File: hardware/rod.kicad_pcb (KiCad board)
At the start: 2 copper layers, 11 parts, among them P1 CONN_01X12, P2 CONN_01X12, P3 GYRO, P4 DOTSTAR, SW1 SW_PUSH_R, SW2 SW_PUSH_G, SW3 SW_PUSH_B

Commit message: Updated PCB
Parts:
- removed BZ1: buzzer, Buzzers_Beepers:MagneticBuzzer_Kingstate_KCG0601
- removed P3: GYRO, Pin_Headers:Pin_Header_Straight_1x05
- added P5: USB_B, Connect:USB_B, F.Cu at (104.1, 170.2)
- P1, P2: value CONN_01X12 -> arduino_mini
- SW1: moved to B.Cu
- SW2: value SW_PUSH_G -> SW_PUSH_B; moved to B.Cu
- SW3: value SW_PUSH_B -> SW_PUSH_G; moved to B.Cu
- moved SW2 34.4 mm to (104.1, 130.8), turned to 90 degrees
- moved SW1 31.9 mm to (104.1, 113.0), turned to 90 degrees
- moved P1 29.6 mm to (119.4, 59.7)
- moved SW3 28.1 mm to (104.1, 148.6), turned to 90 degrees
- moved R1 24.0 mm to (119.4, 106.7), turned to 270 degrees
- moved P2 18.3 mm to (101.6, 59.7)
- moved R2 17.3 mm to (116.8, 123.2), turned to 270 degrees
- moved R3 14.5 mm to (119.4, 143.5), turned to 270 degrees
- moved P4 12.0 mm to (114.3, 49.5), turned to 270 degrees
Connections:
- P1 pad 5: Net-(P1-Pad5) -> A3
- P2 pad 4: GND -> Net-(P2-Pad4)
- P2 pad 6: e -> 3
- P4 pad 2: 6 -> 3
- P4 pad 3: 7 -> 2
- R1 pad 2: 4 -> 6
- R2 pad 2: 3 -> 5
- R3 pad 2: 2 -> 4
- SW1 pad 2: 4 -> 6
- SW2 pad 2: 3 -> 5
- SW3 pad 2: 2 -> 4
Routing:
- net PWR: track 0.00 -> 174.4 mm
- net GND: track 0.00 -> 170.9 mm
- net TX: track 0.00 -> 136.8 mm
- net RX: track 0.00 -> 129.0 mm
- net 4: track 0.00 -> 98.5 mm
- net 5: track 0.00 -> 72.8 mm
- net 6: track 0.00 -> 52.3 mm
- net 3: track 0.00 -> 30.0 mm
- net 2: track 0.00 -> 25.7 mm

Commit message: Updated PCB
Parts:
- moved P5 7.18 mm to (109.2, 175.3), turned to 270 degrees
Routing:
- net PWR: track 174.4 -> 211.3 mm
- net RX: track 129.0 -> 135.1 mm
- net TX: track 136.8 -> 140.4 mm
- net 6: track 52.3 -> 51.2 mm

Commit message: "Updated PCB"
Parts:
- moved R1 4.02 mm to (115.6, 108.0)
- moved R3 3.81 mm to (115.6, 143.5)
- moved R2 2.84 mm to (115.6, 125.7)
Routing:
- net GND: track 170.7 -> 162.9 mm
- net 6: track 51.2 -> 46.1 mm
- net 4: track 98.5 -> 94.7 mm
- net 5: track 72.8 -> 72.0 mm
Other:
- board outline added: 61 x 154.9 mm

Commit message: bak file created
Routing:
- net PWR: track 211.3 -> 176.5 mm
- net TX: track 140.4 -> 136.1 mm
- net GND: track 162.9 -> 159.3 mm
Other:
- board size 61 x 154.9 mm -> 40.6 x 149.9 mm
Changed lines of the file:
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@@
     (links 27)
     (no_connects 7)
-    (area 87.304999 41.584999 133.675002 190.735001)
+    (area 78.664999 35.484999 139.775001 190.575001)
     (thickness 1.6)
-    (drawings 4)
-    (tracks 93)
+    (drawings 6)
+    (tracks 94)
     (zones 0)
     (modules 10)
@@
       (outputformat 1)
       (mirror false)
-      (drillshape 1)
+      (drillshape 0)
       (scaleselection 1)
       (outputdirectory ""))
@@
     )
   )
-  (gr_line (start 78.74 190.5) (end 78.74 35.56) (angle 90) (layer Edge.Cuts) (width 0.15))
-  (gr_line (start 139.7 190.5) (end 78.74 190.5) (angle 90) (layer Edge.Cuts) (width 0.15))
-  (gr_line (start 139.7 35.56) (end 139.7 190.5) (angle 90) (layer Edge.Cuts) (width 0.15))
-  (gr_line (start 78.74 35.56) (end 139.7 35.56) (angle 90) (layer Edge.Cuts) (width 0.15))
-  (segment (start 115.57 125.73) (end 119.38 121.92) (width 0.25) (layer F.Cu) (net 2) (status 400000))
-  (segment (start 118.11 107.95) (end 115.57 107.95) (width 0.25) (layer F.Cu) (net 2) (status 800000))
+  (gr_line (start 91.44 190.5) (end 128.27 190.5) (angle 90) (layer Edge.Cuts) (width 0.15))
+  (gr_line (start 87.63 40.64) (end 128.27 40.64) (angle 90) (layer Edge.Cuts) (width 0.15))
+  (gr_line (start 87.63 190.5) (end 91.44 190.5) (angle 90) (layer Edge.Cuts) (width 0.15))
+  (gr_line (start 87.63 40.64) (end 87.63 190.5) (angle 90) (layer Edge.Cuts) (width 0.15))
+  (gr_line (start 128.27 187.96) (end 128.27 190.5) (angle 90) (layer Edge.Cuts) (width 0.15))
+  (gr_line (start 128.27 40.64) (end 128.27 187.96) (angle 90) (layer Edge.Cuts) (width 0.15))
+  (segment (start 114.3 49.53) (end 120.65 49.53) (width 0.25) (layer F.Cu) (net 2) (status 400000))
+  (segment (start 120.65 62.23) (end 119.38 62.23) (width 0.25) (layer F.Cu) (net 2) (status 800000))
+  (segment (start 121.92 60.96) (end 120.65 62.23) (width 0.25) (layer F.Cu) (net 2))
+  (segment (start 121.92 50.8) (end 121.92 60.96) (width 0.25) (layer F.Cu) (net 2))
+  (segment (start 120.65 49.53) (end 121.92 50.8) (width 0.25) (layer F.Cu) (net 2))
+  (segment (start 115.57 125.73) (end 119.38 121.92) (width 0.25) (layer F.Cu) (net 2))
+  (segment (start 118.11 107.95) (end 115.57 107.95) (width 0.25) (layer F.Cu) (net 2))
   (segment (start 119.38 109.22) (end 118.11 107.95) (width 0.25) (layer F.Cu) (net 2))
   (segment (start 119.38 121.92) (end 119.38 109.22) (width 0.25) (layer F.Cu) (net 2))
@@
   (segment (start 116.84 62.23) (end 119.38 62.23) (width 0.25) (layer F.Cu) (net 2))
   (segment (start 115.57 63.5) (end 116.84 62.23) (width 0.25) (layer F.Cu) (net 2))
-  (segment (start 114.3 49.53) (end 121.92 49.53) (width 0.25) (layer F.Cu) (net 2))
-  (segment (start 121.92 62.23) (end 119.38 62.23) (width 0.25) (layer F.Cu) (net 2))
-  (segment (start 124.46 59.69) (end 121.92 62.23) (width 0.25) (layer F.Cu) (net 2))
-  (segment (start 124.46 52.07) (end 124.46 59.69) (width 0.25) (layer F.Cu) (net 2))
-  (segment (start 121.92 49.53) (end 124.46 52.07) (width 0.25) (layer F.Cu) (net 2))
-  (segment (start 113.03 46.99) (end 115.57 44.45) (width 0.25) (layer F.Cu) (net 5))
+  (segment (start 120.65 44.45) (end 125.73 49.53) (width 0.25) (layer F.Cu) (net 5))
+  (segment (start 125.73 64.77) (end 123.19 67.31) (width 0.25) (layer F.Cu) (net 5))
+  (segment (start 125.73 49.53) (end 125.73 64.77) (width 0.25) (layer F.Cu) (net 5))
+  (segment (start 119.38 45.72) (end 124.46 50.8) (width 0.25) (layer F.Cu) (net 5))
+  (segment (start 124.46 63.5) (end 121.92 66.04) (width 0.25) (layer F.Cu) (net 5))
+  (segment (start 124.46 50.8) (end 124.46 63.5) (width 0.25) (layer F.Cu) (net 5))
+  (segment (start 106.68 45.72) (end 107.95 44.45) (width 0.25) (layer F.Cu) (net 5))
+  (segment (start 107.95 44.45) (end 120.65 44.45) (width 0.25) (layer F.Cu) (net 5))
+  (segment (start 114.3 45.72) (end 119.38 45.72) (width 0.25) (layer F.Cu) (net 5))
+  (segment (start 113.03 46.99) (end 114.3 45.72) (width 0.25) (layer F.Cu) (net 5))
   (segment (start 120.65 66.04) (end 119.38 67.31) (width 0.25) (layer F.Cu) (net 5))
-  (segment (start 125.73 66.04) (end 120.65 66.04) (width 0.25) (layer F.Cu) (net 5))
-  (segment (start 130.81 60.96) (end 125.73 66.04) (width 0.25) (layer F.Cu) (net 5))
-  (segment (start 130.81 46.99) (end 130.81 60.96) (width 0.25) (layer F.Cu) (net 5))
-  (segment (start 128.27 44.45) (end 130.81 46.99) (width 0.25) (layer F.Cu) (net 5))
-  (segment (start 115.57 44.45) (end 128.27 44.45) (width 0.25) (layer F.Cu) (net 5))
-  (segment (start 106.68 46.99) (end 106.68 44.45) (width 0.25) (layer F.Cu) (net 5))
-  (segment (start 129.54 67.31) (end 119.38 67.31) (width 0.25) (layer F.Cu) (net 5))
-  (segment (start 133.35 63.5) (end 129.54 67.31) (width 0.25) (layer F.Cu) (net 5))
-  (segment (start 133.35 44.45) (end 133.35 63.5) (width 0.25) (layer F.Cu) (net 5))
-  (segment (start 130.81 41.91) (end 133.35 44.45) (width 0.25) (layer F.Cu) (net 5))
-  (segment (start 109.22 41.91) (end 130.81 41.91) (width 0.25) (layer F.Cu) (net 5))
-  (segment (start 106.68 44.45) (end 109.22 41.91) (width 0.25) (layer F.Cu) (net 5))
+  (segment (start 121.92 66.04) (end 120.65 66.04) (width 0.25) (layer F.Cu) (net 5))
+  (segment (start 106.68 46.99) (end 106.68 45.72) (width 0.25) (layer F.Cu) (net 5))
+  (segment (start 123.19 67.31) (end 119.38 67.31) (width 0.25) (layer F.Cu) (net 5))
   (segment (start 106.68 49.53) (end 106.68 46.99) (width 0.25) (layer F.Cu) (net 5))
   (segment (start 106.68 154.94) (end 110.49 158.75) (width 0.25) (layer F.Cu) (net 5))
@@
   (segment (start 106.68 72.39) (end 101.6 72.39) (width 0.25) (layer F.Cu) (net 21))
   (segment (start 111.76 67.31) (end 106.68 72.39) (width 0.25) (layer F.Cu) (net 21))
+  (segment (start 95.25 59.69) (end 90.17 64.77) (width 0.25) (layer F.Cu) (net 23))
+  (segment (start 90.17 167.64) (end 91.44 168.91) (width 0.25) (layer F.Cu) (net 23))
+  (segment (start 90.17 64.77) (end 90.17 167.64) (width 0.25) (layer F.Cu) (net 23))
   (segment (start 106.68 175.26) (end 104.14 172.72) (width 0.25) (layer F.Cu) (net 23))
-  (segment (start 95.25 172.72) (end 87.63 165.1) (width 0.25) (layer F.Cu) (net 23))
-  (segment (start 87.63 165.1) (end 87.63 63.5) (width 0.25) (layer F.Cu) (net 23))
-  (segment (start 87.63 63.5) (end 91.44 59.69) (width 0.25) (layer F.Cu) (net 23))
-  (segment (start 91.44 59.69) (end 101.6 59.69) (width 0.25) (layer F.Cu) (net 23))
+  (segment (start 95.25 172.72) (end 91.44 168.91) (width 0.25) (layer F.Cu) (net 23))
   (segment (start 104.14 172.72) (end 95.25 172.72) (width 0.25) (layer F.Cu) (net 23))
+  (segment (start 95.25 59.69) (end 101.6 59.69) (width 0.25) (layer F.Cu) (net 23))
   (segment (start 106.13898 172.17898) (end 107.95 173.99) (width 0.25) (layer F.Cu) (net 24))
   (segment (start 101.6 62.23) (end 95.25 62.23) (width 0.25) (layer F.Cu) (net 24))

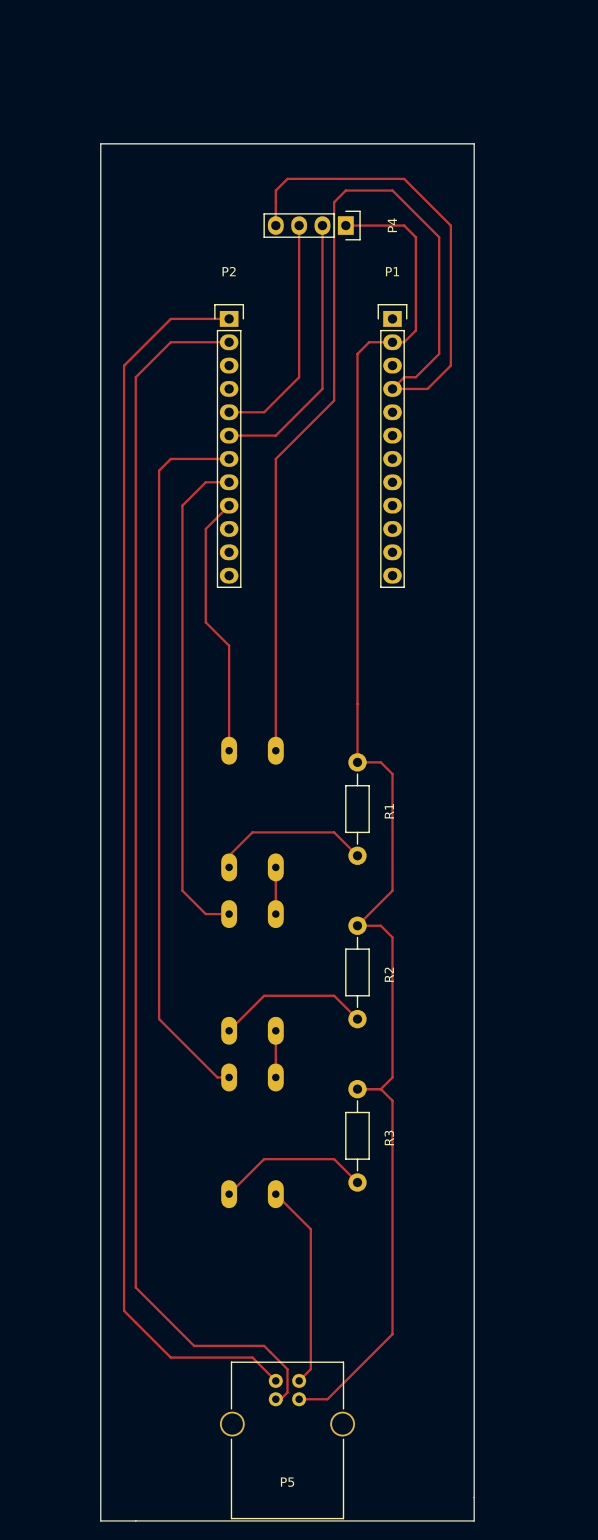
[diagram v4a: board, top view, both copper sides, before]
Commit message: 3.6cm width pcb
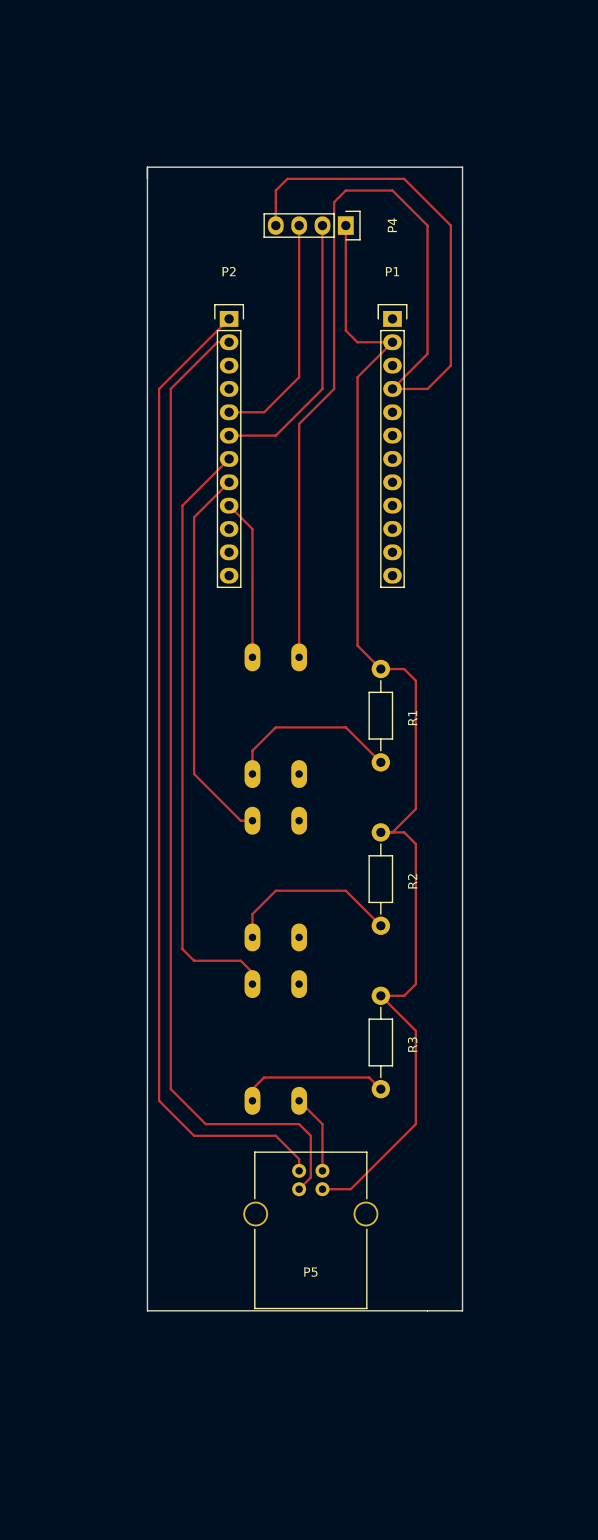
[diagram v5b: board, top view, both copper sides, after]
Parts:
- moved P5 23.0 mm to (111.8, 152.4)
- moved R2 10.5 mm to (118.1, 115.6)
- moved R1 10.5 mm to (118.1, 97.8)
- moved R3 10.5 mm to (118.1, 133.3)
- moved SW1 10.5 mm to (106.7, 102.9)
- moved SW2 10.5 mm to (106.7, 120.7)
- moved SW3 10.5 mm to (106.7, 138.4)
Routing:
- net PWR: track 176.5 -> 139.5 mm
- net TX: track 136.1 -> 107.4 mm
- net GND: track 159.3 -> 130.9 mm
- net RX: track 135.1 -> 108.9 mm
- net 4: track 94.7 -> 81.7 mm
- net 5: track 72.0 -> 62.2 mm
- net 6: track 46.1 -> 38.0 mm
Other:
- board size 40.6 x 149.9 mm -> 34.3 x 124.5 mm

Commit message: updated semi-final version of rod pcb schematics and layout
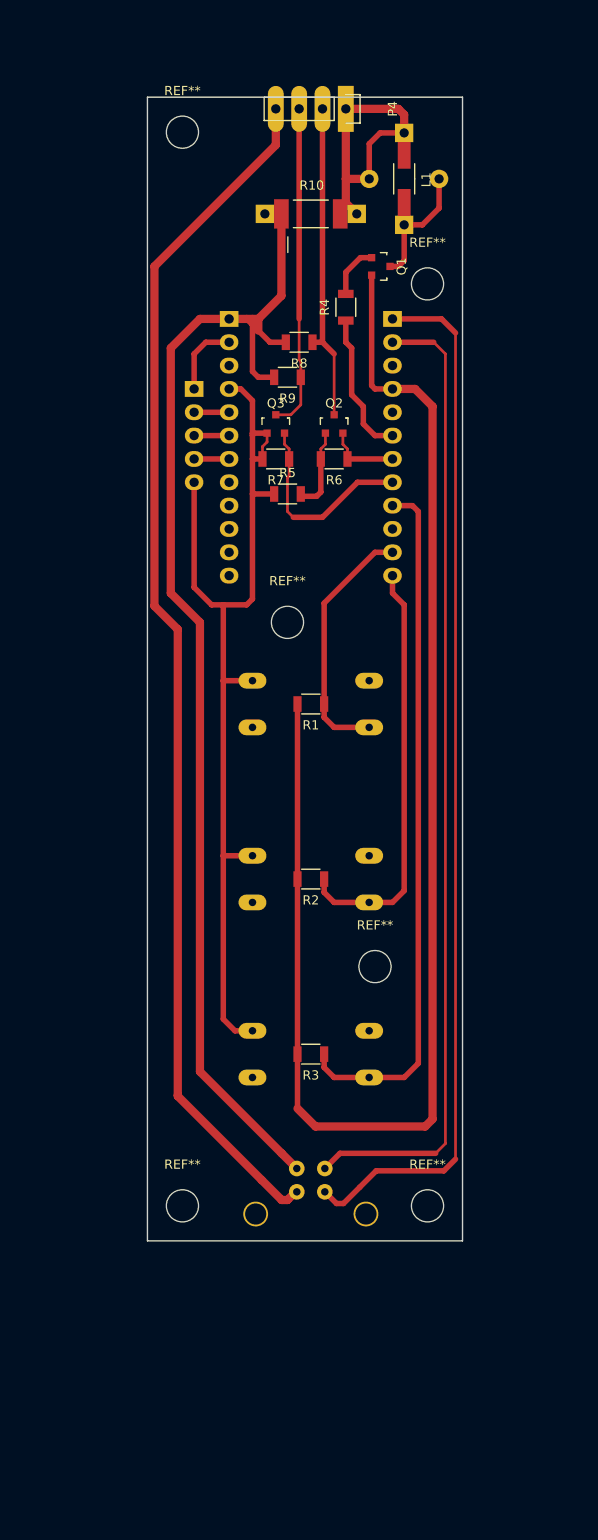
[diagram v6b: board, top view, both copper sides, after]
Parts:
- added BZ1: buzzer, Buzzers_Beepers:Buzzer_12x9.5RM7.6, B.Cu at (120.7, 44.5)
- added L1: INDUCTOR_SMALL, Resistors_Universal:Resistor_SMD+THTuniversal_1206_RM10_HandSoldering, F.Cu at (120.7, 44.5)
- added P3: GYRO, Pin_Headers:Pin_Header_Straight_1x05, B.Cu at (97.8, 67.3)
- added Q1: MMBT3904, TO_SOT_Packages_SMD:SOT-23, F.Cu at (118.1, 54.0)
- added Q2: BSS138, TO_SOT_Packages_SMD:SOT-23, F.Cu at (113.0, 71.1)
- added Q3: BSS138, TO_SOT_Packages_SMD:SOT-23, F.Cu at (106.7, 71.1)
- added R10: 0, Resistors_Universal:Resistor_SMD+THTuniversal_2512_RM10_HandSoldering, F.Cu at (110.5, 48.3)
- added R4: 1K, Resistors_SMD:R_1206, F.Cu at (114.3, 58.4)
- added R5: 0, Resistors_SMD:R_1206, F.Cu at (108.0, 78.7)
- added R6: 10K, Resistors_SMD:R_1206, F.Cu at (113.0, 74.9)
- added R7: 10K, Resistors_SMD:R_1206, F.Cu at (106.7, 74.9)
- added R8: 1K, Resistors_SMD:R_1206, F.Cu at (109.2, 62.2)
- added R9: 1K, Resistors_SMD:R_1206, F.Cu at (108.0, 66.0)
- added REF**: MountingHole_3-5mm, Mounting_Holes:MountingHole_3-5mm, F.Cu at (123.2, 156.2)
- added REF**: MountingHole_3-5mm, Mounting_Holes:MountingHole_3-5mm, F.Cu at (123.2, 55.9)
- added REF**: MountingHole_3-5mm, Mounting_Holes:MountingHole_3-5mm, F.Cu at (117.5, 130.2)
- added REF**: MountingHole_3-5mm, Mounting_Holes:MountingHole_3-5mm, F.Cu at (108.0, 92.7)
- added REF**: MountingHole_3-5mm, Mounting_Holes:MountingHole_3-5mm, F.Cu at (96.5, 156.2)
- added REF**: MountingHole_3-5mm, Mounting_Holes:MountingHole_3-5mm, F.Cu at (96.5, 39.4)
- P1, P2: value arduino_mini -> CONN_01X12; moved to B.Cu
- P5: moved to B.Cu
- R1, R2, R3: value R -> 10K; footprint Resistors_ThroughHole:Resistor_Horizontal_RM10mm -> Resistors_SMD:R_1206
- SW2: value SW_PUSH_B -> SW_PUSH_G
- SW3: value SW_PUSH_G -> SW_PUSH_B
- moved P1 17.8 mm to (101.6, 59.7), turned to 180 degrees
- moved P2 17.8 mm to (119.4, 59.7), turned to 180 degrees
- moved P4 12.7 mm to (114.3, 36.8)
- moved R3 9.92 mm to (110.5, 139.7), turned to 180 degrees
- moved R2 9.16 mm to (110.5, 120.7), turned to 180 degrees
- moved R1 8.52 mm to (110.5, 101.6), turned to 180 degrees
- moved SW1 4.02 mm to (110.5, 101.6), turned to 180 degrees
- moved SW3 4.02 mm to (110.5, 139.7), turned to 180 degrees
- moved SW2 3.81 mm to (110.5, 120.7), turned to 180 degrees
- moved P5 2.54 mm to (109.2, 152.4)
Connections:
- P1 pad 1: Net-(P1-Pad1) -> V50
- P1 pad 10: 12 -> (no net)
- P1 pad 11: 11 -> (no net)
- P1 pad 12: 10 -> (no net)
- P1 pad 3: Net-(P1-Pad3) -> (no net)
- P1 pad 4: PWR -> V33
- P1 pad 8: A0 -> (no net)
- P1 pad 9: 13 -> (no net)
- P2 pad 1: TX -> TX(Weapon)
- P2 pad 10: 7 -> (no net)
- P2 pad 11: 8 -> D8
- P2 pad 12: 9 -> D9
- P2 pad 2: RX -> RX(Weapon)
- P2 pad 3: Net-(P2-Pad3) -> (no net)
- P2 pad 4: Net-(P2-Pad4) -> GND
- P2 pad 5: 2 -> (no net)
- P2 pad 6: 3 -> D3
- P2 pad 7: 4 -> D4
- P2 pad 8: 5 -> D5
- P2 pad 9: 6 -> D6
- P4 pad 1: GND -> V50
- P4 pad 2: 3 -> CLOCK_IN
- P4 pad 3: 2 -> DATA_IN
- P4 pad 4: PWR -> GND
- P5 pad 1: PWR -> V50
- P5 pad 2: TX -> RX(Weapon)
- P5 pad 3: RX -> TX(Weapon)
- R1 pad 1: GND -> D8
- R1 pad 2: 6 -> GND
- R2 pad 1: GND -> D9
- R2 pad 2: 5 -> GND
- R3 pad 1: GND -> D6
- R3 pad 2: 4 -> GND
- SW1 pad 1: PWR -> V33
- SW1 pad 2: 6 -> D8
- SW2 pad 1: PWR -> V33
- SW2 pad 2: 5 -> D9
- SW3 pad 1: PWR -> V33
- SW3 pad 2: 4 -> D6
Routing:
- net GND: track 130.9 -> 297.1 mm
- net V50: track 0.00 -> 163.7 mm
- net PWR: track 139.5 -> 0.00 mm
- net V33: track 0.00 -> 115.7 mm
- net TX(Weapon): track 0.00 -> 114.3 mm
- net RX: track 108.9 -> 0.00 mm
- net TX: track 107.4 -> 0.00 mm
- net RX(Weapon): track 0.00 -> 106.5 mm
- net 4: track 81.7 -> 0.00 mm
- net D6: track 0.00 -> 75.9 mm
- net 5: track 62.2 -> 0.00 mm
- net D9: track 0.00 -> 46.0 mm
- net 6: track 38.0 -> 0.00 mm
- net DATA_IN: track 0.00 -> 35.4 mm
- net CLOCK_IN: track 0.00 -> 34.9 mm
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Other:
- outline, holes or cut-outs redrawn
- net class Default: clearance 0.2 -> 0.8; trace_width 0.25 -> 0.3
- rule trace_clearance: 0.2 -> 0.8
